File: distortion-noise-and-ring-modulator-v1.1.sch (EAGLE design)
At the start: 75 parts, among them IC1 TL074JT, IC2 TL074JT, IC3 LM13700SL, Q1 MMBT3906, T1 NOISE-2N3904, U1 MC1496DR2G, X1 MA06-1JN, X2 MA06-1JN

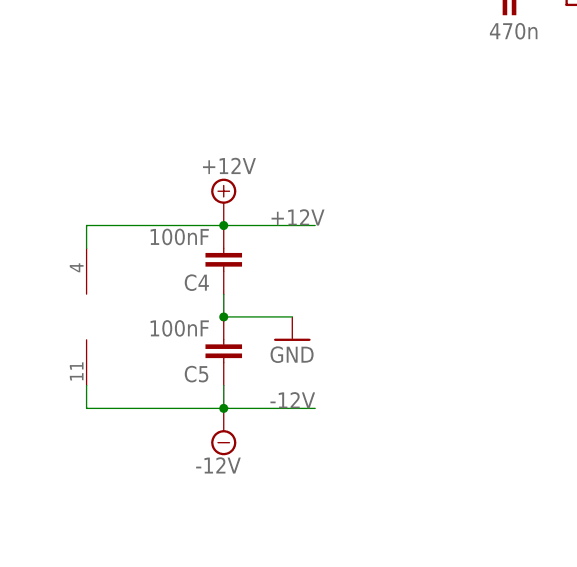
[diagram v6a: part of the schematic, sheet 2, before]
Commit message: Fixed 1uF caps
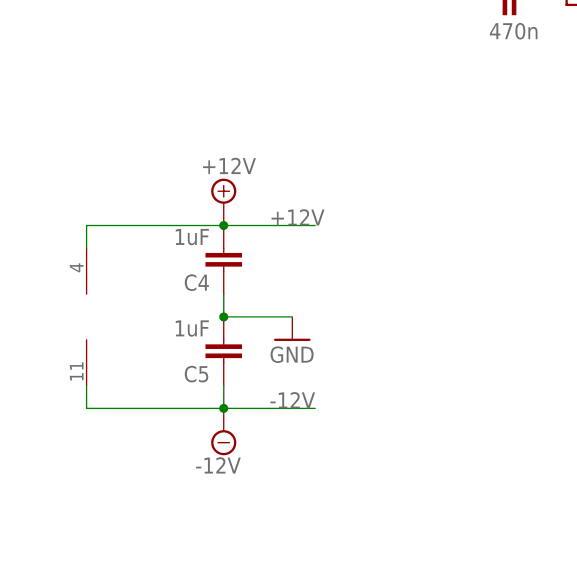
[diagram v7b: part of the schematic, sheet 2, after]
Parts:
- C1: value 100n -> 1uF
- C15, C16, C4, C5: value 100nF -> 1uF
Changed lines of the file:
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@@
 <part name="GND6" library="supply1" library_urn="urn:adsk.eagle:library:371" deviceset="GND" device=""/>
 <part name="GND7" library="supply1" library_urn="urn:adsk.eagle:library:371" deviceset="GND" device=""/>
-<part name="C1" library="joakim" deviceset="C-EU-J" device="0402" value="100n"/>
+<part name="C1" library="joakim" deviceset="C-EU-J" device="0402" value="1uF"/>
 <part name="GND8" library="supply1" library_urn="urn:adsk.eagle:library:371" deviceset="GND" device=""/>
 <part name="R24" library="rcl" library_urn="urn:adsk.eagle:library:334" deviceset="R-EU_" device="R0402" package3d_urn="urn:adsk.eagle:package:23547/3" value="220k"/>
@@
 <part name="C14" library="joakim" deviceset="C-EU-J" device="0402" value="2n2"/>
 <part name="IC2" library="joakim" deviceset="TL074J" device="T"/>
-<part name="C4" library="joakim" deviceset="C-EU-J" device="0402" value="100nF"/>
+<part name="C4" library="joakim" deviceset="C-EU-J" device="0402" value="1uF"/>
 <part name="GND9" library="supply1" deviceset="GND" device=""/>
 <part name="GND10" library="supply1" deviceset="GND" device=""/>
@@
 <part name="SUPPLY10" library="supply2" library_urn="urn:adsk.eagle:library:372" deviceset="-12V" device=""/>
 <part name="SUPPLY11" library="supply2" library_urn="urn:adsk.eagle:library:372" deviceset="+12V" device=""/>
-<part name="C5" library="joakim" deviceset="C-EU-J" device="0402" value="100nF"/>
+<part name="C5" library="joakim" deviceset="C-EU-J" device="0402" value="1uF"/>
 <part name="R42" library="rcl" library_urn="urn:adsk.eagle:library:334" deviceset="R-EU_" device="R0402" package3d_urn="urn:adsk.eagle:package:23547/3" value="33k"/>
 <part name="R43" library="rcl" library_urn="urn:adsk.eagle:library:334" deviceset="R-EU_" device="R0402" package3d_urn="urn:adsk.eagle:package:23547/3" value="1k"/>
@@
 <part name="D1" library="joakim" deviceset="1N4148" device="SOD323" package3d_urn="urn:adsk.eagle:package:30992/2" value="1N4148"/>
 <part name="IC3" library="joakim" deviceset="LM13700" device="SL"/>
-<part name="C15" library="joakim" deviceset="C-EU-J" device="0402" value="100nF"/>
-<part name="C16" library="joakim" deviceset="C-EU-J" device="0402" value="100nF"/>
+<part name="C15" library="joakim" deviceset="C-EU-J" device="0402" value="1uF"/>
+<part name="C16" library="joakim" deviceset="C-EU-J" device="0402" value="1uF"/>
 <part name="Q1" library="transistor-pnp" library_urn="urn:adsk.eagle:library:399" deviceset="MMBT3906*" device="SMD" package3d_urn="urn:adsk.eagle:package:28748/2" technology="LT1" value="MMBT3906"/>
 <part name="R41" library="rcl" library_urn="urn:adsk.eagle:library:334" deviceset="R-EU_" device="R0402" package3d_urn="urn:adsk.eagle:package:23547/3" value="8k2"/>
